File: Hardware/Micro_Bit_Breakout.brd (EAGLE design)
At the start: 68.6 x 22.9 mm, 75 parts, among them J2 CONN_22_NOSILK, U1 micro:bit

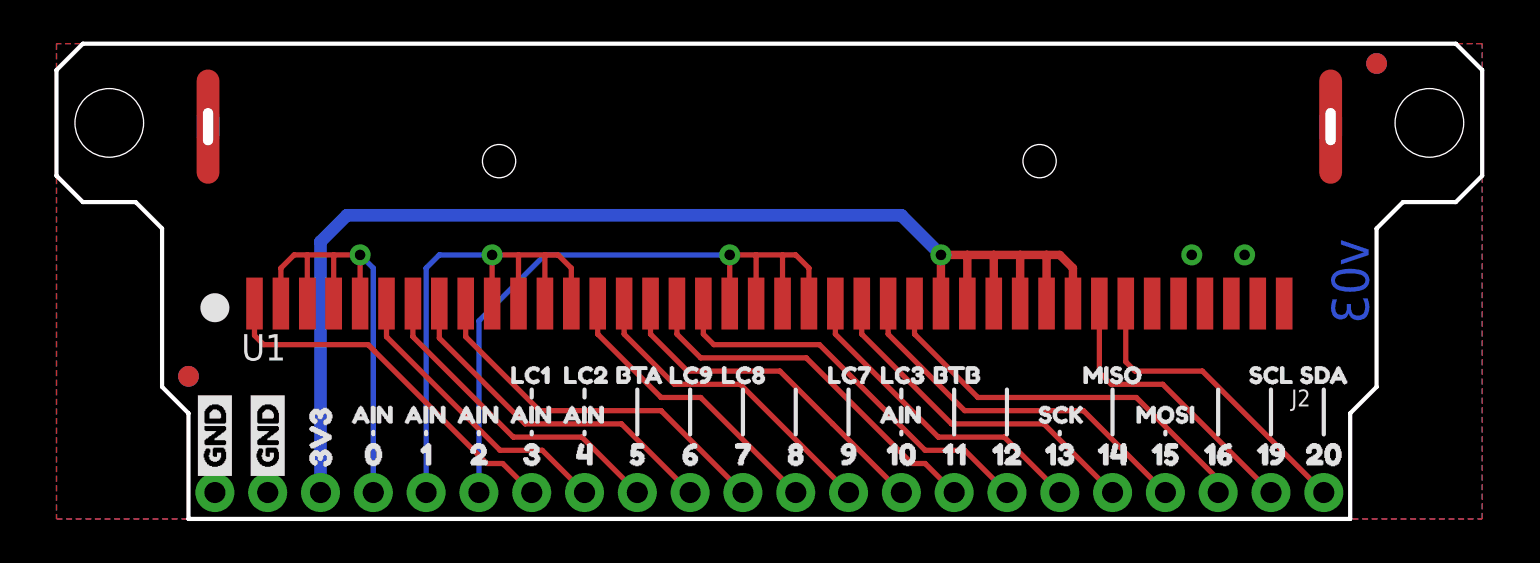
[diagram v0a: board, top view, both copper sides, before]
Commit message: Added Qwiic Connectors
Added virtical qwiic connectors
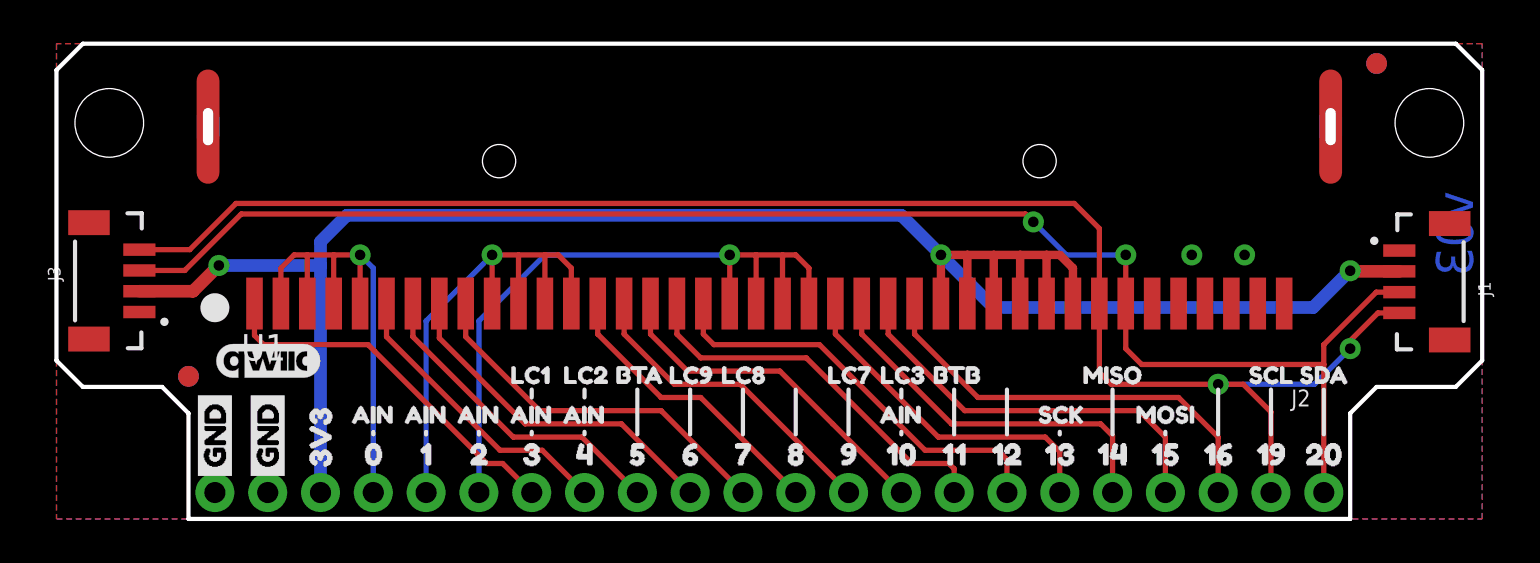
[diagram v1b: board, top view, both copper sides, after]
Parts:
- added J1, J3: Qwiic, SparkFun-Connectors:JST04_1MM_VERT
- added LOGO1: QWIIC_LOGO_5MM, SparkFun-Aesthetics:QWIIC_5MM
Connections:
- net 19: now also J1.4, J3.4
- net 20: now also J1.3, J3.3
- net 3.3V: now also J1.2, J3.2
- net GND: now also J1.1, J3.1
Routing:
- net 19: track 14.0 -> 77.8 mm, vias 0 -> 2
- net 20: track 14.9 -> 75.5 mm, vias 0 -> 2
- net 3.3V: track 63.2 -> 96.3 mm, vias 1 -> 3
- net 14: track 16.7 -> 18.3 mm
- net 15: track 18.0 -> 19.5 mm
- net 1: track 27.0 -> 25.5 mm
- net 16: track 19.6 -> 20.8 mm
- net 13: track 15.4 -> 16.6 mm
- net 12: track 19.2 -> 20.2 mm
- net 11: track 18.0 -> 18.6 mm
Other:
- outline, holes or cut-outs redrawn

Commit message: Update Micro_Bit_Breakout.brd
Moved the Qwiic logo
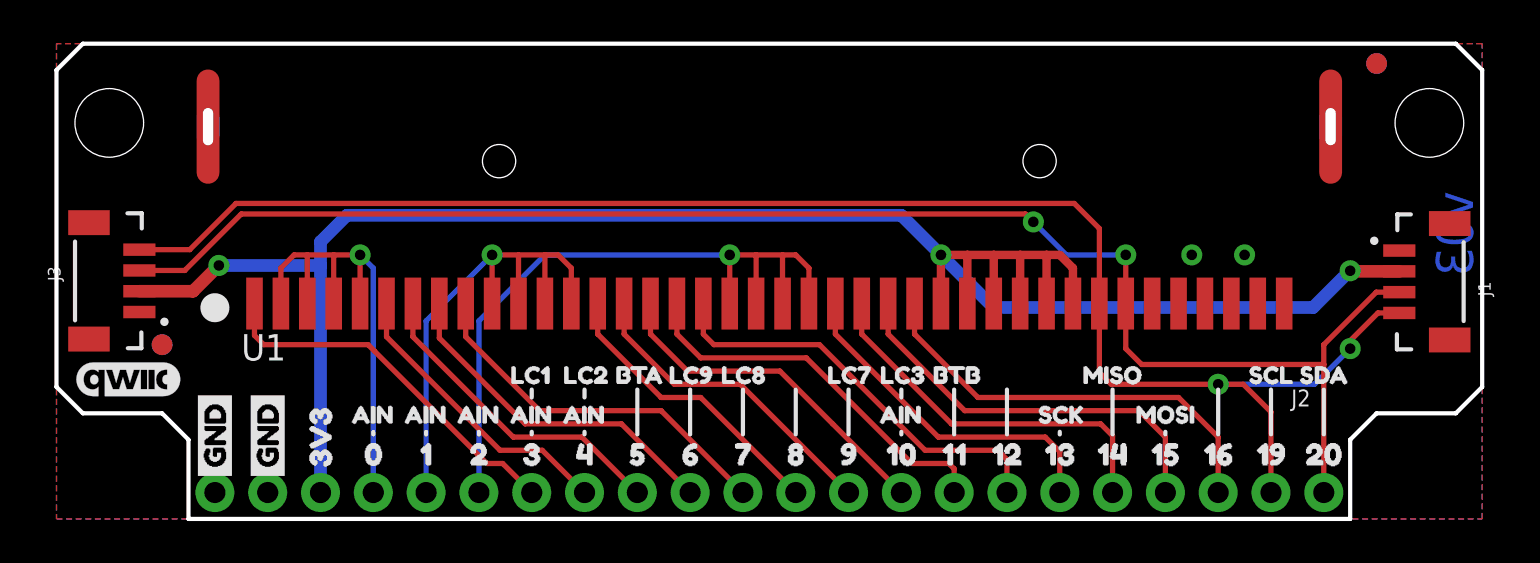
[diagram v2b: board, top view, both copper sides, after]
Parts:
- moved LOGO1 6.79 mm to (3.43, 6.73)
- moved FD1 1.98 mm to (5.08, 8.38)
- moved FD3 1.98 mm to (5.08, 8.38)
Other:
- outline, holes or cut-outs redrawn
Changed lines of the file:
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@@
 <board>
 <plain>
-<wire x1="62.23" y1="0" x2="62.23" y2="5.08" width="0.2032" layer="20"/>
-<wire x1="62.23" y1="5.08" x2="63.5" y2="6.35" width="0.2032" layer="20"/>
-<wire x1="63.5" y1="6.35" x2="67.31" y2="6.35" width="0.2032" layer="20"/>
-<wire x1="1.27" y1="6.35" x2="5.08" y2="6.35" width="0.2032" layer="20"/>
-<wire x1="5.08" y1="6.35" x2="6.35" y2="5.08" width="0.2032" layer="20"/>
-<wire x1="6.35" y1="5.08" x2="6.35" y2="0" width="0.2032" layer="20"/>
+<wire x1="68.58" y1="21.59" x2="68.58" y2="6.35" width="0.2032" layer="20"/>
+<wire x1="68.58" y1="6.35" x2="67.31" y2="5.08" width="0.2032" layer="20"/>
+<wire x1="67.31" y1="5.08" x2="63.5" y2="5.08" width="0.2032" layer="20"/>
+<wire x1="63.5" y1="5.08" x2="62.23" y2="3.81" width="0.2032" layer="20"/>
+<wire x1="62.23" y1="3.81" x2="62.23" y2="0" width="0.2032" layer="20"/>
+<wire x1="0" y1="21.59" x2="0" y2="6.35" width="0.2032" layer="20"/>
+<wire x1="0" y1="6.35" x2="1.27" y2="5.08" width="0.2032" layer="20"/>
+<wire x1="1.27" y1="5.08" x2="5.08" y2="5.08" width="0.2032" layer="20"/>
+<wire x1="5.08" y1="5.08" x2="6.35" y2="3.81" width="0.2032" layer="20"/>
+<wire x1="6.35" y1="3.81" x2="6.35" y2="0" width="0.2032" layer="20"/>
 <wire x1="6.35" y1="0" x2="62.23" y2="0" width="0.2032" layer="20"/>
 <wire x1="67.31" y1="22.86" x2="1.27" y2="22.86" width="0.2032" layer="20"/>
 <wire x1="1.27" y1="22.86" x2="0" y2="21.59" width="0.2032" layer="20"/>
-<wire x1="0" y1="21.59" x2="0" y2="7.62" width="0.2032" layer="20"/>
-<wire x1="0" y1="7.62" x2="1.27" y2="6.35" width="0.2032" layer="20"/>
-<wire x1="68.58" y1="21.59" x2="68.58" y2="7.62" width="0.2032" layer="20"/>
-<wire x1="68.58" y1="7.62" x2="67.31" y2="6.35" width="0.2032" layer="20"/>
 <wire x1="67.31" y1="22.86" x2="68.58" y2="21.59" width="0.2032" layer="20"/>
 <text x="31.75" y="-24.13" size="1.778" layer="51" font="vector" ratio="15">Shawn Hymel</text>
@@
 <dimension x1="2.54" y1="19.05" x2="2.54" y2="22.86" x3="-6.35" y3="20.955" textsize="1.27" layer="47" unit="inch"/>
 <text x="13.97" y="-27.94" size="1.778" layer="51" font="vector">Revised by: Alex Wende</text>
-<dimension x1="62.23" y1="0" x2="62.23" y2="6.35" x3="71.12" y3="3.175" textsize="1.27" layer="47" dtype="vertical" unit="inch"/>
-<dimension x1="67.31" y1="6.35" x2="67.31" y2="22.86" x3="71.12" y3="14.605" textsize="1.27" layer="47" dtype="vertical" unit="inch"/>
+<dimension x1="62.23" y1="0" x2="67.31" y2="5.08" x3="71.12" y3="2.54" textsize="1.27" layer="47" dtype="vertical" unit="inch"/>
+<dimension x1="67.31" y1="5.08" x2="67.31" y2="22.86" x3="71.12" y3="13.97" textsize="1.27" layer="47" dtype="vertical" unit="inch"/>
 <dimension x1="0" y1="7.62" x2="6.35" y2="7.62" x3="3.175" y3="-3.81" textsize="1.27" layer="47" dtype="vertical" unit="inch"/>
 <dimension x1="6.35" y1="0" x2="62.23" y2="0" x3="34.29" y3="-3.81" textsize="1.27" layer="47" dtype="vertical" unit="inch" visible="yes"/>
@@
 <attribute name="VALUE" x="5.969" y="0.508" size="0.8128" layer="27" font="vector" ratio="18" rot="R90"/>
 </element>
-<element name="FD1" library="SparkFun-Aesthetics" package="FIDUCIAL-1X2" value="FIDUCIAL1X2" x="6.35" y="6.858" smashed="yes"/>
+<element name="FD1" library="SparkFun-Aesthetics" package="FIDUCIAL-1X2" value="FIDUCIAL1X2" x="5.08" y="8.382" smashed="yes"/>
 <element name="FD2" library="SparkFun-Aesthetics" package="FIDUCIAL-1X2" value="FIDUCIAL1X2" x="63.5" y="21.9075" smashed="yes"/>
 <element name="H1" library="SparkFun-Electromechanical" package="STAND-OFF" value="STAND-OFF" x="2.54" y="19.05" smashed="yes"/>
@@
 <element name="LOGO3" library="SparkFun-Aesthetics" package="OSHW-LOGO-M" value="OSHW-LOGOM" x="11.684" y="16.002" smashed="yes" rot="MR0"/>
 <element name="LOGO2" library="SparkFun-Aesthetics" package="SFE_LOGO_NAME_FLAME_.1" value="SFE_LOGO_NAME_FLAME.1_INCH" x="40.1955" y="17.018" smashed="yes" rot="MR0"/>
-<element name="FD3" library="SparkFun-Aesthetics" package="FIDUCIAL-1X2" value="FIDUCIAL1X2" x="6.35" y="6.858" smashed="yes" rot="MR0"/>
+<element name="FD3" library="SparkFun-Aesthetics" package="FIDUCIAL-1X2" value="FIDUCIAL1X2" x="5.08" y="8.382" smashed="yes" rot="MR0"/>
 <element name="FD4" library="SparkFun-Aesthetics" package="FIDUCIAL-1X2" value="FIDUCIAL1X2" x="63.5" y="21.9075" smashed="yes" rot="MR0"/>
 <element name="U1" library="SparkFun-Connectors" package="MICRO:BIT-RA_SMD" value="micro:bit" x="34.29" y="16.51" smashed="yes">
@@
 <attribute name="VALUE" x="6.05883125" y="11.446" size="0.6096" layer="27" rot="R90"/>
 </element>
-<element name="LOGO1" library="SparkFun-Aesthetics" package="QWIIC_5MM" value="QWIIC_LOGO_5MM" x="10.16" y="7.62" smashed="yes"/>
+<element name="LOGO1" library="SparkFun-Aesthetics" package="QWIIC_5MM" value="QWIIC_LOGO_5MM" x="3.429" y="6.731" smashed="yes"/>
 </elements>
 <signals>
